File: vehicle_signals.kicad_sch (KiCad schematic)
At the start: 34 parts, among them IC4 TLIN1027DRQ1, U10 G3VM-61VY2, U11 G3VM-61VY2, U12 G3VM-61VY2, U13 G3VM-61VY2, U14 G3VM-61VY2, U15 G3VM-61VY2, U16 G3VM-61VY2, U17 G3VM-61VY2

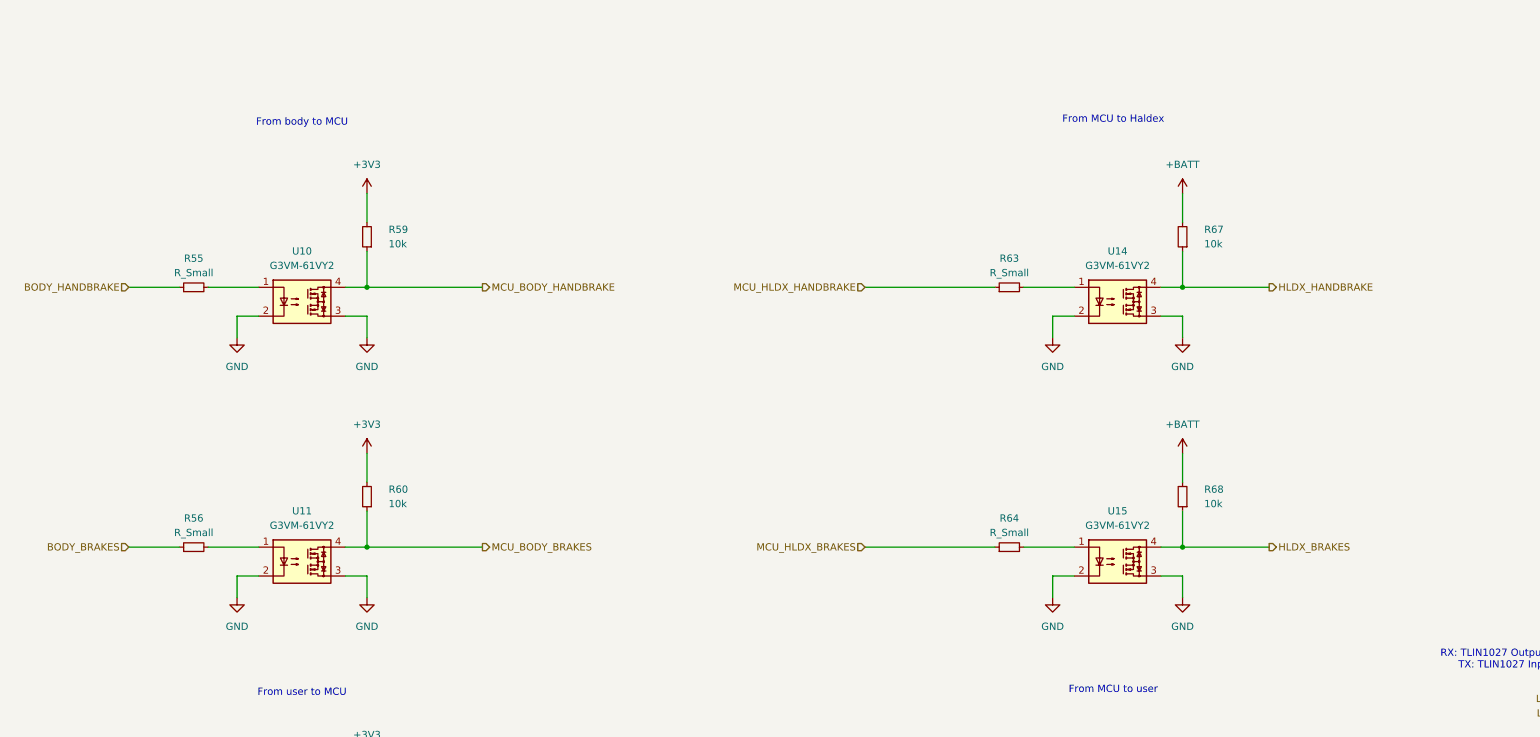
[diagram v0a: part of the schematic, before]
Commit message: sch: fix handbrake/brake I/O
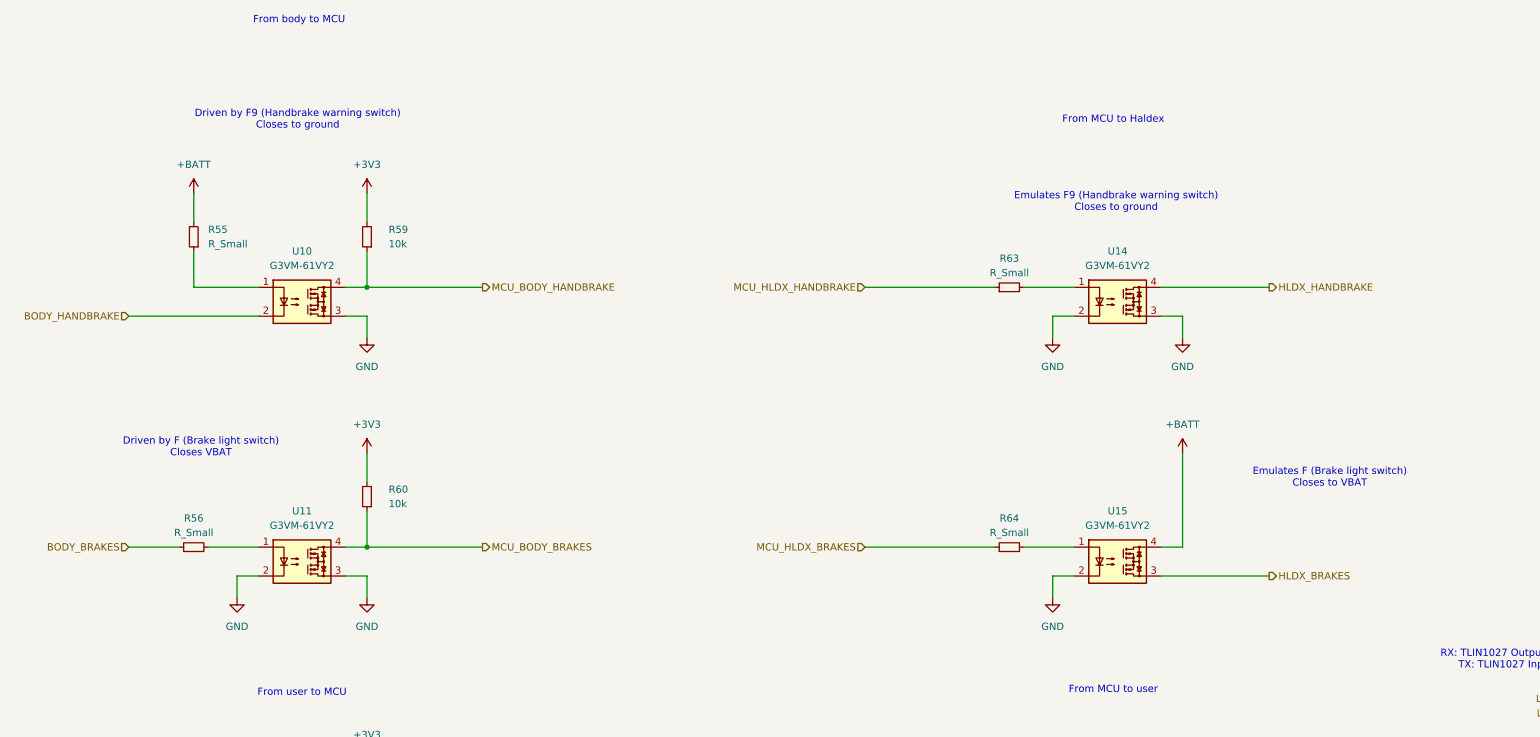
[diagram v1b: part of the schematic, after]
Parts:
- removed R67, R68: 10k, Resistor_SMD:R_0603_1608Metric_Pad0.98x0.95mm_HandSolder, symbol Device:R_Small
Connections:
- net +BATT: now also R55.2, U15.4
- net BODY_HANDBRAKE: now also U10.2; no longer R55.1
- net GND: no longer U10.2, U15.3
- net HLDX_BRAKES: now also U15.3; no longer U15.4
- net at U10.1: now also R55.1; no longer R55.2
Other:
- note added: "Driven by F (Brake light switch) Closes VBAT"
- note added: "Driven by F9 (Handbrake warning switch) Closes to ground"
- note added: "Emulates F (Brake light switch) Closes to VBAT"
- note added: "Emulates F9 (Handbrake warning switch) Closes to ground"
- moved on the sheet: R55
